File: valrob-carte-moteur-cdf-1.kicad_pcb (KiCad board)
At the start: 2 copper layers, 63 x 50 mm, 85 parts, among them J1 USB_C_Receptacle_USB2.0_14P, J2 Conn_01x02, J3 Conn_01x02, J4 Conn_01x04_Pin, J5 Conn_01x08, J6 Conn_01x02, J7 Conn_01x02, J8 Conn_01x08, SW1 SW_Push, SW2 SW_Push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

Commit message: pcb: add uart routing
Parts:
- moved C5 2.61 mm to (109.2, 108.0)
- moved R5 2.61 mm to (109.2, 110.0)
- moved SW2 2.61 mm to (109.2, 113.0)
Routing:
- net /U0RXD: track 0.00 -> 10.5 mm
- net /U0TXD: track 0.00 -> 7.04 mm
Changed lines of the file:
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@@
 	(footprint "Resistor_SMD:R_0603_1608Metric"
 		(layer "F.Cu")
-		(at 110 107.5 180)
+		(at 109.25 110 180)
 		(descr "Resistor SMD 0603 (1608 Metric), square (rectangular) end terminal, IPC-7351 nominal, (Body size source: IPC-SM-782 page 72, https://www.pcb-3d.com/wordpress/wp-content/uploads/ipc-sm-782a_amendment_1_and_2.pdf), generated with kicad-footprint-generator")
 		(tags "resistor")
@@
 	(footprint "Button_Switch_SMD:SW_SPST_TS-1088-xR020"
 		(layer "F.Cu")
-		(at 110 110.5)
+		(at 109.25 113)
 		(descr "SMD Tactile Switch, 3.9x3x2 mm, https://lcsc.com/datasheet/lcsc_datasheet_2504101957_XUNPU-TS-1088-AR02016_C720477.pdf")
 		(tags "Tactile Switch")
@@
 	(footprint "Capacitor_SMD:C_0603_1608Metric"
 		(layer "F.Cu")
-		(at 110 105.5 180)
+		(at 109.25 108 180)
 		(descr "Capacitor SMD 0603 (1608 Metric), square (rectangular) end terminal, IPC-7351 nominal, (Body size source: IPC-SM-782 page 76, https://www.pcb-3d.com/wordpress/wp-content/uploads/ipc-sm-782a_amendment_1_and_2.pdf), generated with kicad-footprint-generator")
 		(tags "capacitor")
@@
 	)
 	(via
-		(at 107.75 105.5)
+		(at 107 108)
 		(size 0.9)
 		(drill 0.4)
@@
 	)
 	(via
-		(at 106.25 110.5)
+		(at 105.5 113)
 		(size 0.9)
 		(drill 0.4)
@@
 	)
 	(segment
+		(start 89.96 94.15)
+		(end 89.96 92.79)
+		(width 0.3)
+		(layer "F.Cu")
+		(net 26)
+	)
+	(segment
+		(start 89.96 92.79)
+		(end 91.25 91.5)
+		(width 0.3)
+		(layer "F.Cu")
+		(net 26)
+	)
+	(segment
+		(start 95 91.5)
+		(end 95.75 90.75)
+		(width 0.3)
+		(layer "F.Cu")
+		(net 26)
+	)
+	(segment
+		(start 96.5 90.75)
+		(end 96.87614 90.37386)
+		(width 0.3)
+		(layer "F.Cu")
+		(net 26)
+	)
+	(segment
+		(start 96.87614 90.37386)
+		(end 96.87614 89.128342)
+		(width 0.3)
+		(layer "F.Cu")
+		(net 26)
+	)
+	(segment
+		(start 95.75 90.75)
+		(end 96.5 90.75)
+		(width 0.3)
+		(layer "F.Cu")
+		(net 26)
+	)
+	(segment
+		(start 91.25 91.5)
+		(end 95 91.5)
+		(width 0.3)
+		(layer "F.Cu")
+		(net 26)
+	)
+	(segment
+		(start 91.79614 90.20386)
+		(end 91.25 90.75)
+		(width 0.3)
+		(layer "F.Cu")
+		(net 27)
+	)
+	(segment
+		(start 91.25 90.75)
+		(end 90 90.75)
+		(width 0.3)
+		(layer "F.Cu")
+		(net 27)
+	)
+	(segment
+		(start 91.79614 89.128342)
+		(end 91.79614 90.20386)
+		(width 0.3)
+		(layer "F.Cu")
+		(net 27)
+	)
+	(segment
+		(start 90 90.75)
+		(end 88.69 92.06)
+		(width 0.3)
+		(layer "F.Cu")
+		(net 27)
+	)
+	(segment
+		(start 88.69 92.06)
+		(end 88.69 94.15)
+		(width 0.3)
+		(layer "F.Cu")
+		(net 27)
+	)
+	(segment

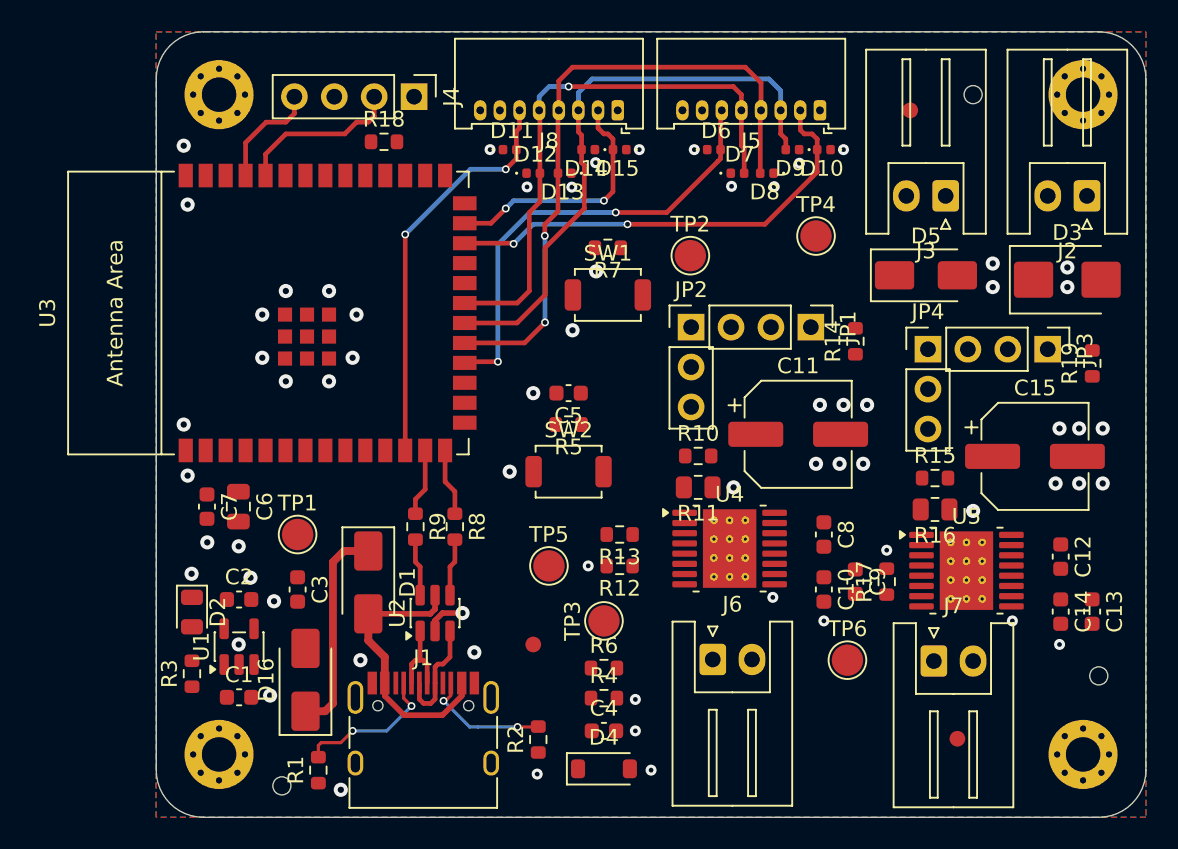
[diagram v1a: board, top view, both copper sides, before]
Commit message: pcb: add DRV8874 dc motor driver routing
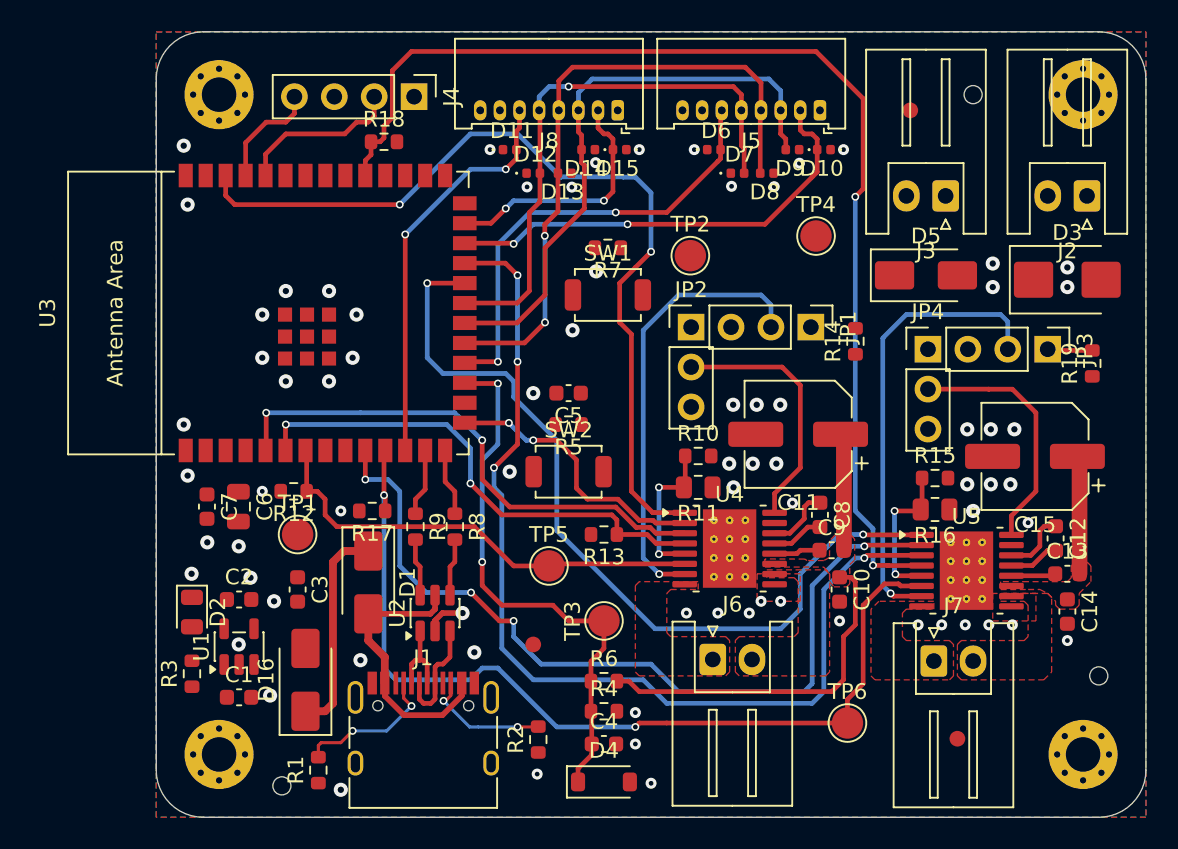
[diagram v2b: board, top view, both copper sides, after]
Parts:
- moved R17 33.1 mm to (96.8, 115.5), turned to 180 degrees
- moved R12 21.3 mm to (91.8, 114.2)
- moved TP6 4.00 mm to (127.0, 129.0)
- moved C13 2.88 mm to (141.0, 119.5), turned to 0 degrees
- moved C9 2.50 mm to (126.0, 118.0), turned to 0 degrees
- moved C8 1.27 mm to (125.2, 115.8)
- moved C12 1.20 mm to (140.2, 117.2)
- moved C10 1.00 mm to (126.5, 120.5)
- moved R13 1.00 mm to (111.5, 117.0)
- moved C4 0.84 mm to (111.5, 130.3)
- moved D4 0.84 mm to (111.5, 132.8)
- moved R4 0.83 mm to (111.5, 128.2)
- moved R6 0.83 mm to (111.5, 126.3)
- moved C14 0.42 mm to (141.0, 121.9)
- turned C11 to 180 degrees
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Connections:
- U3 pad 17: unconnected-(U3-GPIO9/TOUCH9/ADC1_CH8/FSPIHD/SUBSPIHD-Pad17) -> /Vsense
- U3 pad 39: /Vsense -> unconnected-(U3-GPIO1/TOUCH1/ADC1_CH0-Pad39)
- U4 pad 17: (no net) -> GND
- U5 pad 17: (no net) -> GND
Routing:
- net /DC Driver 2/~{FAULT}: track 0.00 -> 72.9 mm, vias 0 -> 2
- net /DC Driver 2/~{SLEEP}: track 0.00 -> 64.1 mm, vias 0 -> 4
- net /DC Driver 2/IPROPI: track 0.00 -> 58.9 mm, vias 0 -> 2
- net /DC Driver/EN/IN1: track 0.00 -> 56.2 mm, vias 0 -> 2
- net /DC Driver 2/PH/IN2: track 0.00 -> 53.7 mm, vias 0 -> 4
- net /DC Driver 2/EN/IN1: track 0.00 -> 53.5 mm, vias 0 -> 2
- net +12V: track 0.00 -> 37.7 mm
- net /Vsense: track 0.00 -> 35.1 mm, vias 0 -> 2
- net /DC Driver/~{SLEEP}: track 0.00 -> 33.7 mm, vias 0 -> 2
- net /DC Driver/~{FAULT}: track 0.00 -> 32.0 mm, vias 0 -> 2
- net /DC Driver/IPROPI: track 0.00 -> 29.3 mm
- net Net-(JP3-C): track 0.00 -> 29.0 mm, vias 0 -> 1
- net Net-(JP1-C): track 0.00 -> 28.3 mm, vias 0 -> 1
- net /DC Driver/PH/IN2: track 0.00 -> 17.7 mm, vias 0 -> 2
- net Net-(JP2-C): track 0.00 -> 16.2 mm
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- added copper zone on F.Cu, net +12V
- added copper zone on F.Cu, net /DC Driver 2/OUT1
- added copper zone on F.Cu, net /DC Driver 2/OUT2
- added copper zone on F.Cu, net /DC Driver/OUT1
- added copper zone on F.Cu, net /DC Driver/OUT2

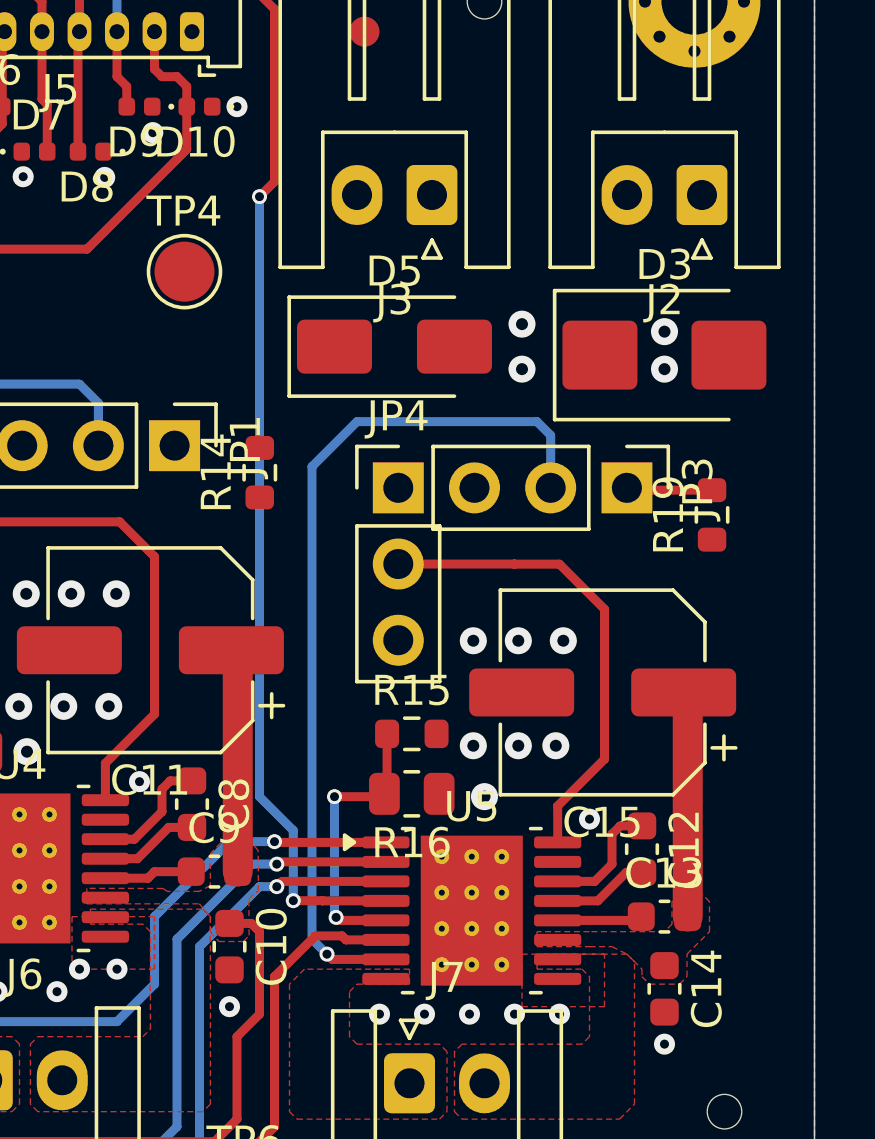
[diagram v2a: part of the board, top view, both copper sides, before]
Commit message: pcb: add 12V routing
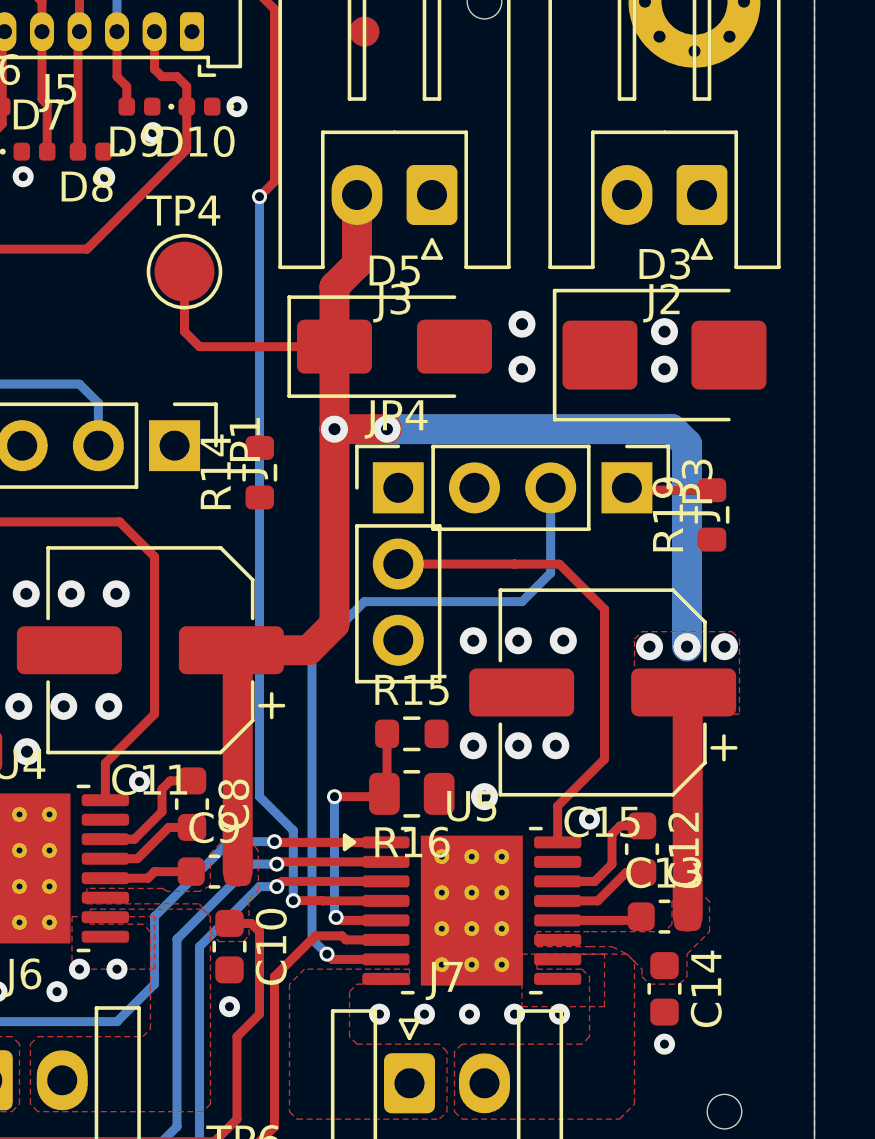
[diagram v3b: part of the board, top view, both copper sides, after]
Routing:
- net +12V: track 37.7 -> 82.0 mm, vias 0 -> 5
- net Net-(JP3-C): track 29.0 -> 24.2 mm
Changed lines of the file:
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@@
 	)
 	(segment
+		(start 125.5 100.5)
+		(end 125 100)
+		(width 0.3)
+		(layer "F.Cu")
+		(net 9)
+	)
+	(segment
 		(start 127.5 120)
 		(end 127.5 122.75)
@@
 	)
 	(segment
+		(start 130 103.25)
+		(end 131.75 103.25)
+		(width 1)
+		(layer "F.Cu")
+		(net 9)
+	)
+	(segment
 		(start 126.775 110.8325)
 		(end 126.5625 110.62)
@@
 	)
 	(segment
+		(start 130 109.75)
+		(end 130 103.25)
+		(width 1)
+		(layer "F.Cu")
+		(net 9)
+	)
+	(segment
+		(start 125 100)
+		(end 125 98)
+		(width 0.3)
+		(layer "F.Cu")
+		(net 9)
+	)
+	(segment
 		(start 141.775 119.5)
 		(end 141.775 112.162715)
@@
 	)
 	(segment
+		(start 130 103.25)
+		(end 130 100.5)
+		(width 1)
+		(layer "F.Cu")
+		(net 9)
+	)
+	(segment
+		(start 130 100.5)
+		(end 130 98.5)
+		(width 1)
+		(layer "F.Cu")
+		(net 9)
+	)
+	(segment
+		(start 126.5625 110.62)
+		(end 129.13 110.62)
+		(width 1)
+		(layer "F.Cu")
+		(net 9)
+	)
+	(segment
 		(start 126.75 126.25)
 		(end 126 127)
@@
 	)
 	(segment
+		(start 130 100.5)
+		(end 125.5 100.5)
+		(width 0.3)
+		(layer "F.Cu")
+		(net 9)
+	)
+	(segment
 		(start 141.775 112.162715)
 		(end 141.63867 112.026385)
@@
 	)
 	(segment
+		(start 129.13 110.62)
+		(end 130 109.75)
+		(width 1)
+		(layer "F.Cu")
+		(net 9)
+	)
+	(segment
 		(start 113.085 126.335)
 		(end 112.325 126.335)
@@
 	)
 	(segment
+		(start 130 98.5)
+		(end 130.75 97.75)
+		(width 1)
+		(layer "F.Cu")
+		(net 9)
+	)
+	(segment
 		(start 126.5 119.725)
 		(end 127.225 119.725)
@@
 	)
 	(segment
+		(start 130.75 97.75)
+		(end 130.75 95.445)
+		(width 1)
+		(layer "F.Cu")
+		(net 9)
+	)
+	(segment
 		(start 127.225 119.725)
 		(end 127.5 120)
@@
 		(net 9)
 	)
+	(via
+		(at 143 110.5)
+		(size 0.9)
+		(drill 0.4)
+		(layers "F.Cu" "B.Cu")
+		(free yes)
+		(net 9)
+	)
+	(via
+		(at 131.75 103.25)
+		(size 0.9)
+		(drill 0.4)
+		(layers "F.Cu" "B.Cu")
+		(net 9)
+	)
+	(via
+		(at 140.5 110.5)
+		(size 0.9)
+		(drill 0.4)
+		(layers "F.Cu" "B.Cu")
+		(free yes)
+		(net 9)
+	)
+	(via
+		(at 130 103.25)
+		(size 0.9)
+		(drill 0.4)
+		(layers "F.Cu" "B.Cu")
+		(net 9)
+	)
+	(via
+		(at 141.75 110.5)
+		(size 0.9)
+		(drill 0.4)
+		(layers "F.Cu" "B.Cu")
+		(free yes)
+		(net 9)
+	)
+	(segment
+		(start 141.75 103.75)
+		(end 141.25 103.25)
+		(width 1)
+		(layer "B.Cu")
+		(net 9)
+	)
+	(segment
+		(start 141.25 103.25)
+		(end 131.75 103.25)
+		(width 1)
+		(layer "B.Cu")
+		(net 9)
+	)
+	(segment
+		(start 141.75 110.5)
+		(end 141.75 103.75)
+		(width 1)
+		(layer "B.Cu")
+		(net 9)
+	)
 	(segment
 		(start 138.775 118.975)
@@
 	)
 	(segment
-		(start 129.25 120.25)
-		(end 129.25 104.5)
+		(start 137.20617 105.206385)
+		(end 137.20617 108.04383)
 		(width 0.3)
 		(layer "B.Cu")
@@
 	)
 	(segment
-		(start 129.25 104.5)
-		(end 130.75 103)
+		(start 131 109)
+		(end 129.25 110.75)
 		(width 0.3)
 		(layer "B.Cu")
@@
 	)
 	(segment
-		(start 129.75 120.75)
-		(end 129.25 120.25)
+		(start 136.25 109)
+		(end 131 109)
 		(width 0.3)
 		(layer "B.Cu")
@@
 	)
 	(segment
-		(start 130.75 103)
-		(end 136.75 103)
+		(start 129.25 120.25)
+		(end 129.75 120.75)
 		(width 0.3)
 		(layer "B.Cu")
@@
 	)
 	(segment
-		(start 137.20617 103.45617)
-		(end 137.20617 105.206385)
+		(start 137.20617 108.04383)
+		(end 136.25 109)
 		(width 0.3)
 		(layer "B.Cu")
@@
 	)
 	(segment
-		(start 136.75 103)
-		(end 137.20617 103.45617)
+		(start 129.25 110.75)
+		(end 129.25 120.25)
 		(width 0.3)
 		(layer "B.Cu")
@@
 			)
 		)
+	)
+	(zone
+		(net 9)
+		(net_name "+12V")
+		(layer "F.Cu")
+		(hatch edge 0.5)
+		(priority 6)
+		(connect_pads yes
+			(clearance 0.2)
+		)
+		(min_thickness 0.15)
+		(filled_areas_thickness no)
+		(fill yes
+			(thermal_gap 0.5)
+			(thermal_bridge_width 0.5)
+		)
+		(polygon
+			(pts
+				(xy 140 112.75) (xy 140 110.25) (xy 140.25 110) (xy 143.25 110) (xy 143.5 110.25) (xy 143.5 112.75)
+			)
+		)

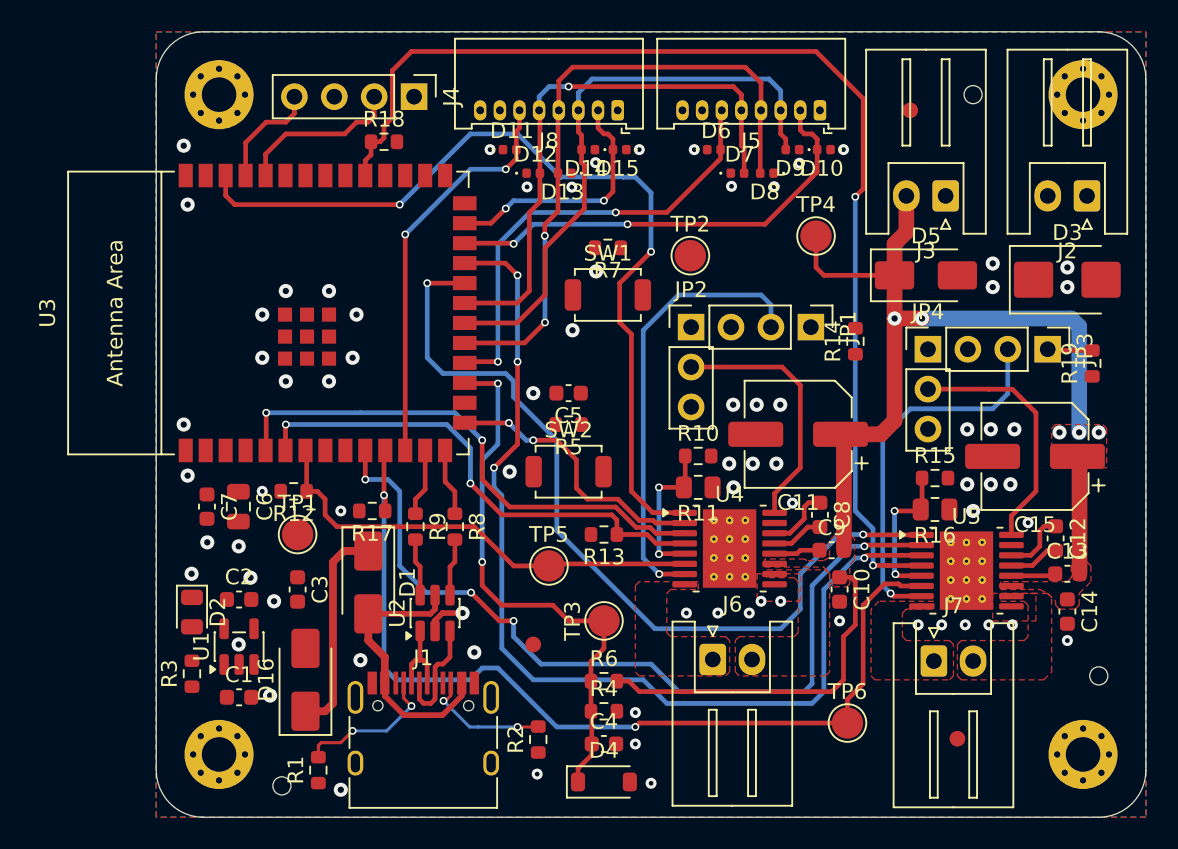
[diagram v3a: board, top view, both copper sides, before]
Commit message: pcb: route power
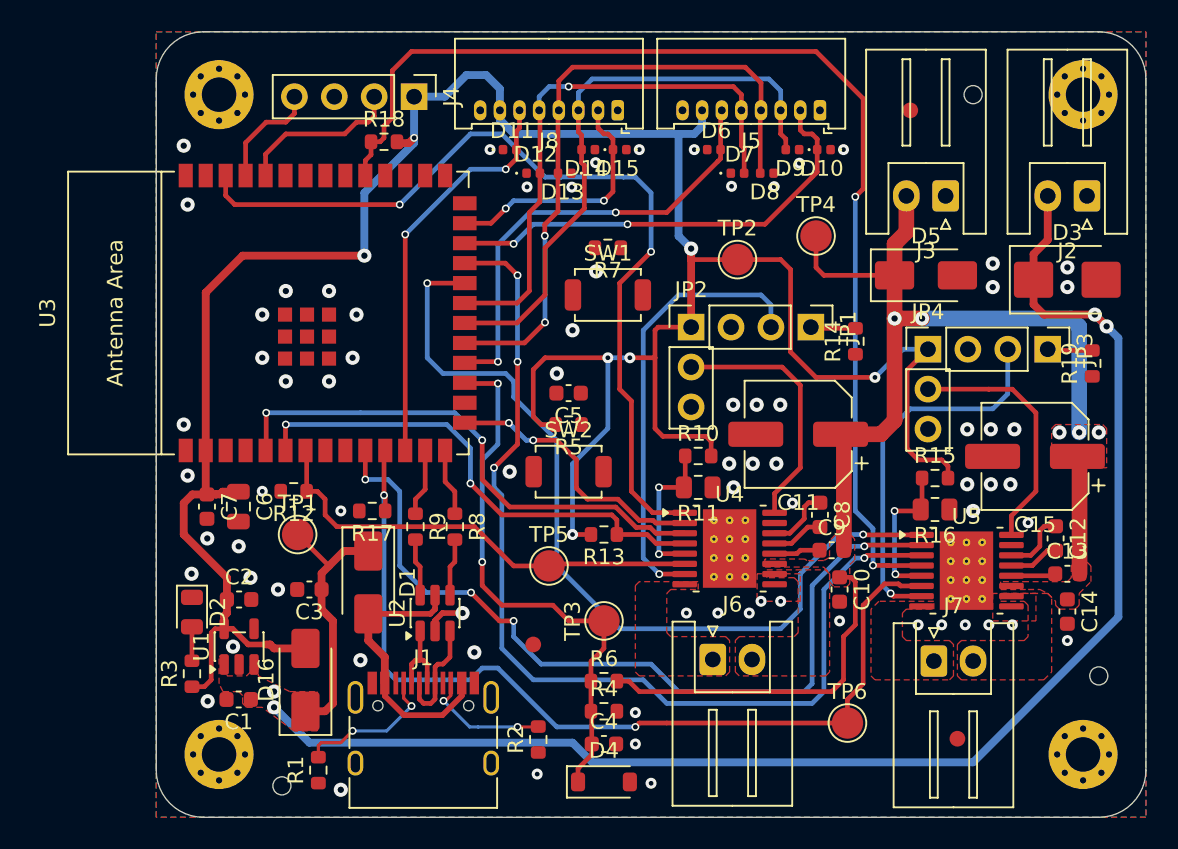
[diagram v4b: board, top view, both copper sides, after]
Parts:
- moved TP2 3.01 mm to (120.0, 99.5)
- moved C3 0.75 mm to (92.8, 120.5), turned to 180 degrees
- moved C1 0.14 mm to (88.2, 127.5), turned to 180 degrees
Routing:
- net +3V3: track 0.00 -> 169.4 mm, vias 0 -> 7
- net +5V: track 13.5 -> 108.3 mm, vias 0 -> 4
- net Net-(JP1-A): track 0.00 -> 2.87 mm
- net Net-(D2-A): track 0.00 -> 2.16 mm
- net /DC Driver 2/EN/IN1: track 53.5 -> 54.8 mm
- added copper zone on F.Cu, net +5V
